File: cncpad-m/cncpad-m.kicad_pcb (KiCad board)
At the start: 2 copper layers, 99.2 x 88 mm, 27 parts, among them J1 Conn_01x04_Male - Encoder, SW1 SW_PUSH, SW2 SW_PUSH, SW3 SW_PUSH, SW4 SW_PUSH, SW5 SW_PUSH, SW6 SW_PUSH, SW7 SW_PUSH, SW8 SW_PUSH, SW9 SW_PUSH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

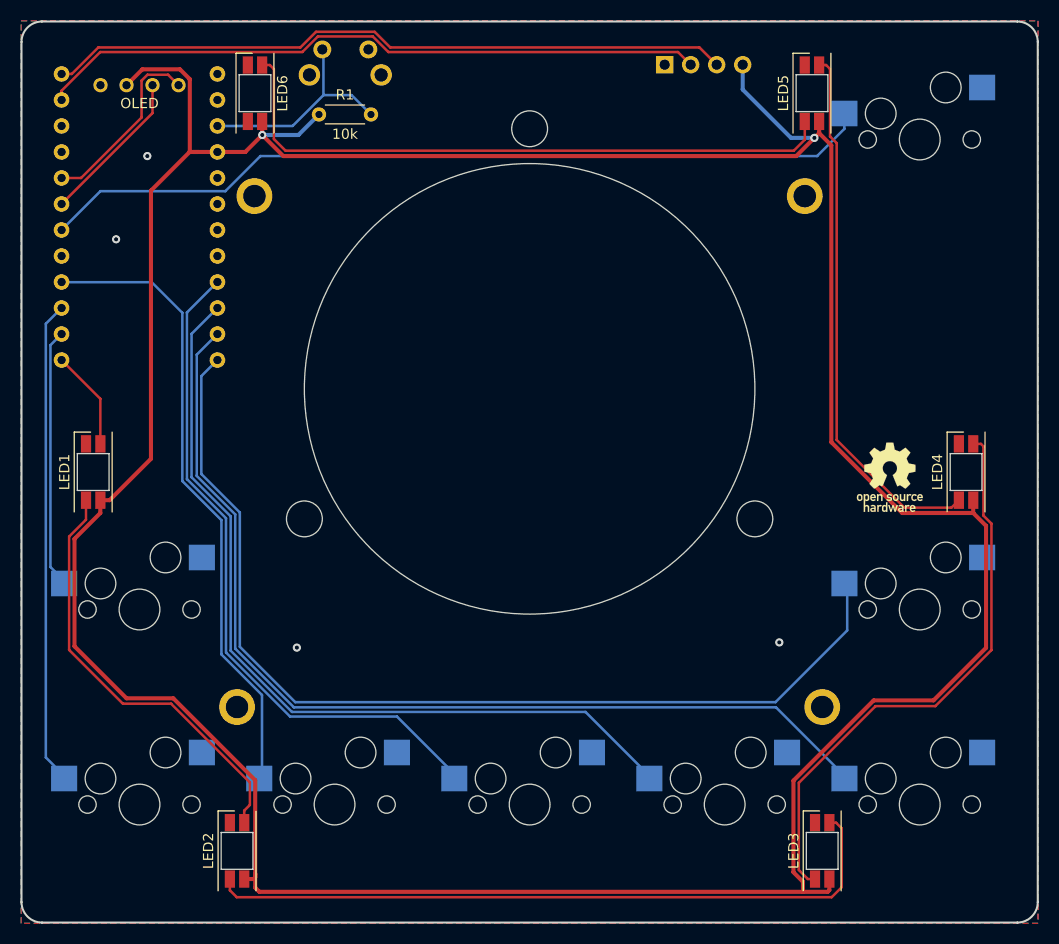
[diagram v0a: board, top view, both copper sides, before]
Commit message: Add missing I2C pullups; change encoder header
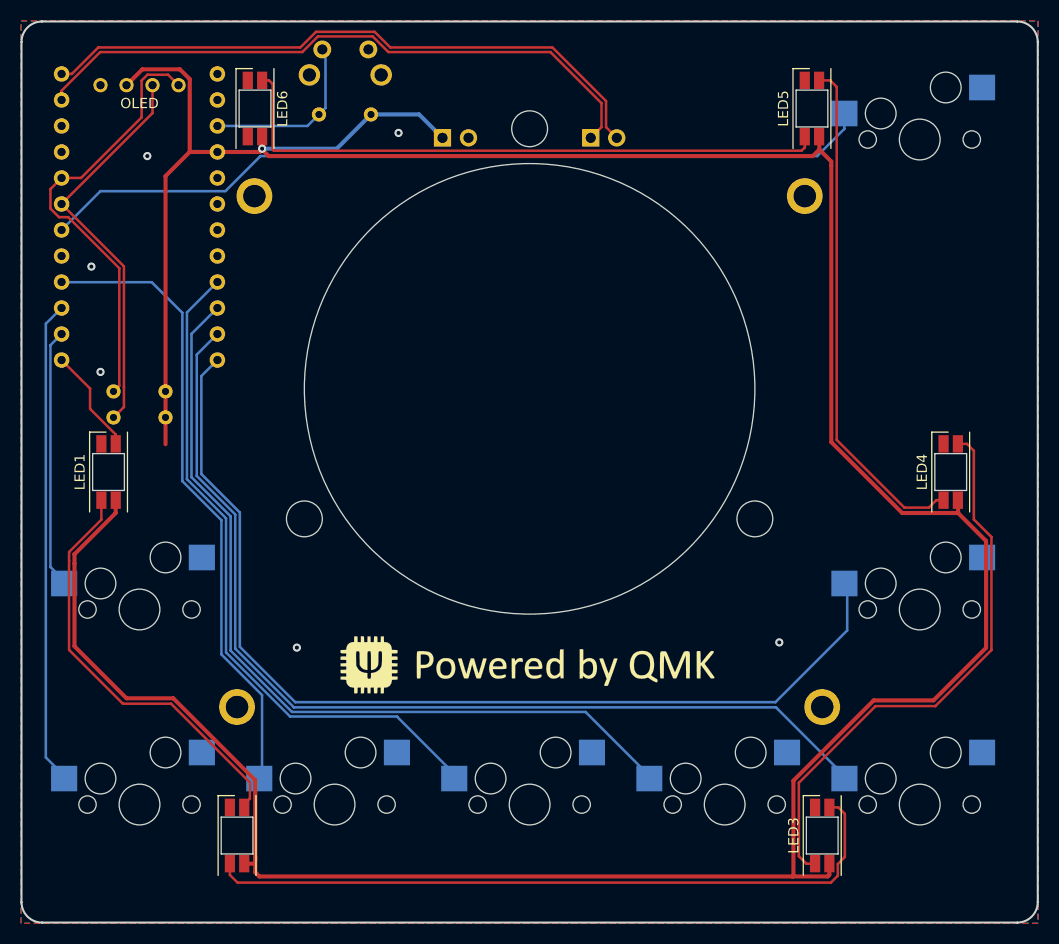
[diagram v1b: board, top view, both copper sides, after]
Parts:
- added J2: Conn_01x02_Male, Connector_PinHeader_2.54mm:PinHeader_1x02_P2.54mm_Horizontal, B.Cu at (158.4, 69.5)
- added R2: 1.5k, Resistor_THT:R_Axial_DIN0204_L3.6mm_D1.6mm_P5.08mm_Horizontal, B.Cu at (116.8, 94.2)
- added R3: 1.5k, Resistor_THT:R_Axial_DIN0204_L3.6mm_D1.6mm_P5.08mm_Horizontal, B.Cu at (116.8, 96.8)
- J1: value Conn_01x04_Male - Encoder -> Conn_01x02_Male; footprint Connector_PinHeader_2.54mm:PinHeader_1x04_P2.54mm_Horizontal -> Connector_PinHeader_2.54mm:PinHeader_1x02_P2.54mm_Horizontal
- LOGO2, R1: moved to B.Cu
- LOGO3: moved to F.Cu
- moved LOGO2 58.0 mm to (142.9, 139.5), turned to 180 degrees
- moved J1 22.8 mm to (143.9, 69.5)
- moved R1 5.08 mm to (136.9, 67.2), turned to 180 degrees
- moved LED1 1.50 mm to (111.3, 102.1)
- moved LED2 1.50 mm to (123.8, 137.6)
- moved LED3 1.50 mm to (181.0, 137.6)
- moved LED4 1.50 mm to (193.5, 102.1)
- moved LED5 1.50 mm to (180.0, 66.6)
- moved LED6 1.50 mm to (125.6, 66.6)
- turned LOGO3 to 0 degrees
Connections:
- J1 pad 1: GND -> +5V
- J1 pad 2: EN2 -> GND
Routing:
- net SDA: track 18.1 -> 43.0 mm
- net SCL: track 15.3 -> 39.1 mm
- net +5V: track 342.7 -> 329.0 mm, vias 2 -> 1
- net EN1: track 67.0 -> 61.7 mm
- net RESET: track 21.5 -> 17.1 mm
- net EN2: track 65.7 -> 62.4 mm
- net Net-(LED4-Pad2): track 52.7 -> 49.9 mm
- net Net-(LED5-Pad2): track 62.7 -> 60.8 mm
- net Net-(LED1-Pad2): track 42.5 -> 41.6 mm
- net Net-(LED3-Pad2): track 56.0 -> 55.2 mm
- net RGB: track 9.76 -> 10.4 mm
- net GND: vias 4 -> 6
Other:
- board text added: "CNCPad Rev0.97 piit79 / 42keebs.eu"
- board text removed: "CNCPad Rev0.95 piit79 / 42keebs.eu 2021"
